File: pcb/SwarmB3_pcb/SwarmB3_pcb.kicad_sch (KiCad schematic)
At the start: 53 parts, among them J1 5v_3Pi, J10 ItsyBitsyRight, J11 ItsyBitsyLeft, J12 ItsyBitsyBottom, J2 GND_3Pi, J3 I2C_3V3_Exp, J4 Conn_02x15_M5Stack_Core2, J5 I2C_3Pi, J6 3PI_SWTCH, J8 ProxA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

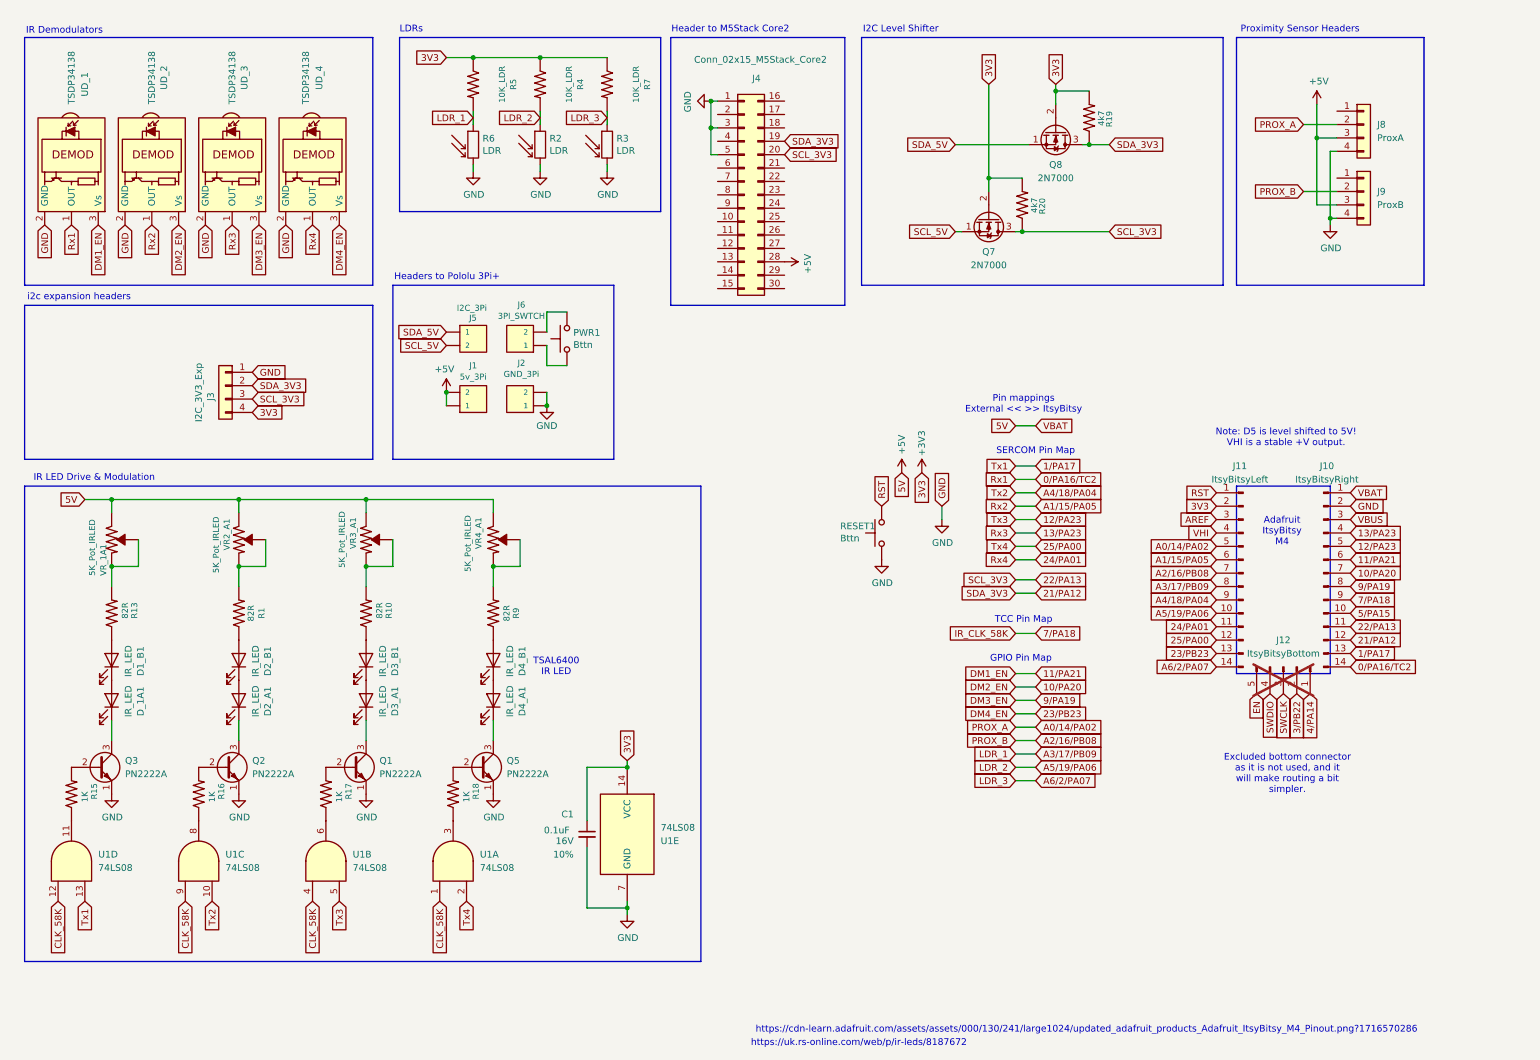
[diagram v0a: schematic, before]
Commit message: add initial test code for itsybitsy
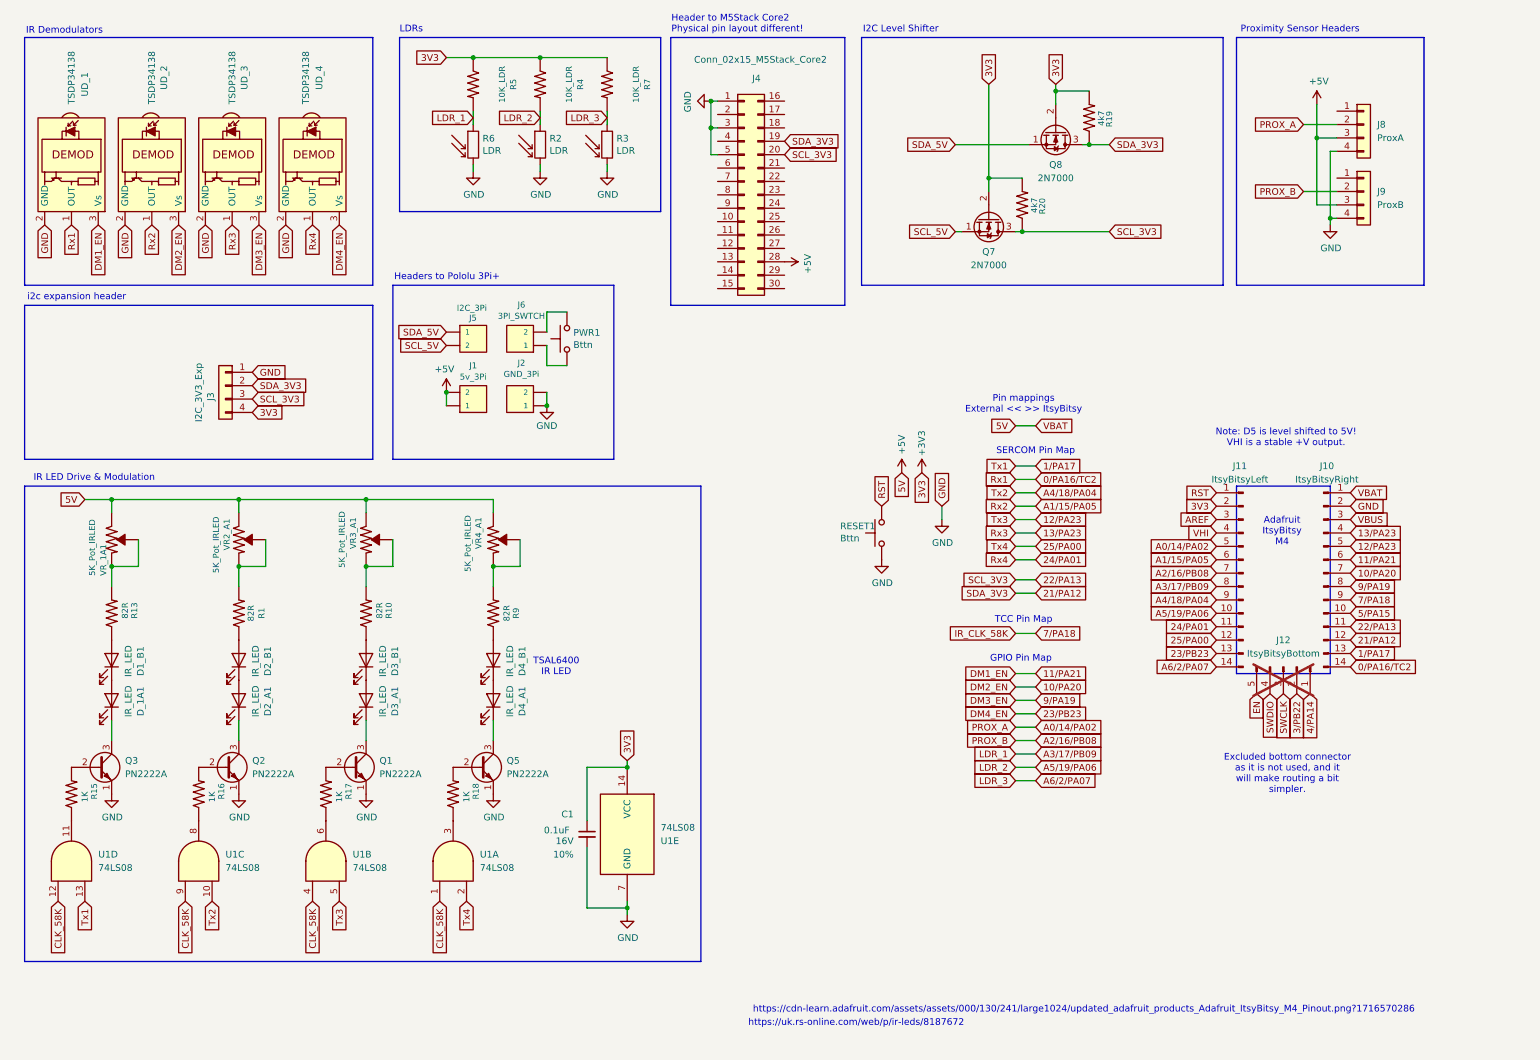
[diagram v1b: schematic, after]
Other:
- note added: "Header to M5Stack Core2 Physical pin layout different!"
- note added: "i2c expansion header"
- note removed: "Header to M5Stack Core2"
- note removed: "i2c expansion headers"
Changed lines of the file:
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@@
 		)
 	)
-	(text "Header to M5Stack Core2\n"
+	(text "Header to M5Stack Core2\nPhysical pin layout different!"
 		(exclude_from_sim no)
 		(at 136.652 17.018 0)
@@
 	(text "https://uk.rs-online.com/web/p/ir-leds/8187672"
 		(exclude_from_sim no)
-		(at 172.212 208.534 0)
+		(at 171.704 204.724 0)
 		(effects
 			(font
@@
 	(text "https://cdn-learn.adafruit.com/assets/assets/000/130/241/large1024/updated_adafruit_products_Adafruit_ItsyBitsy_M4_Pinout.png?1716570286"
 		(exclude_from_sim no)
-		(at 215.392 205.994 0)
+		(at 214.884 202.184 0)
 		(effects
 			(font
@@
 		)
 	)
-	(text "i2c expansion headers\n"
+	(text "i2c expansion header\n"
 		(exclude_from_sim no)
 		(at 14.478 67.818 0)

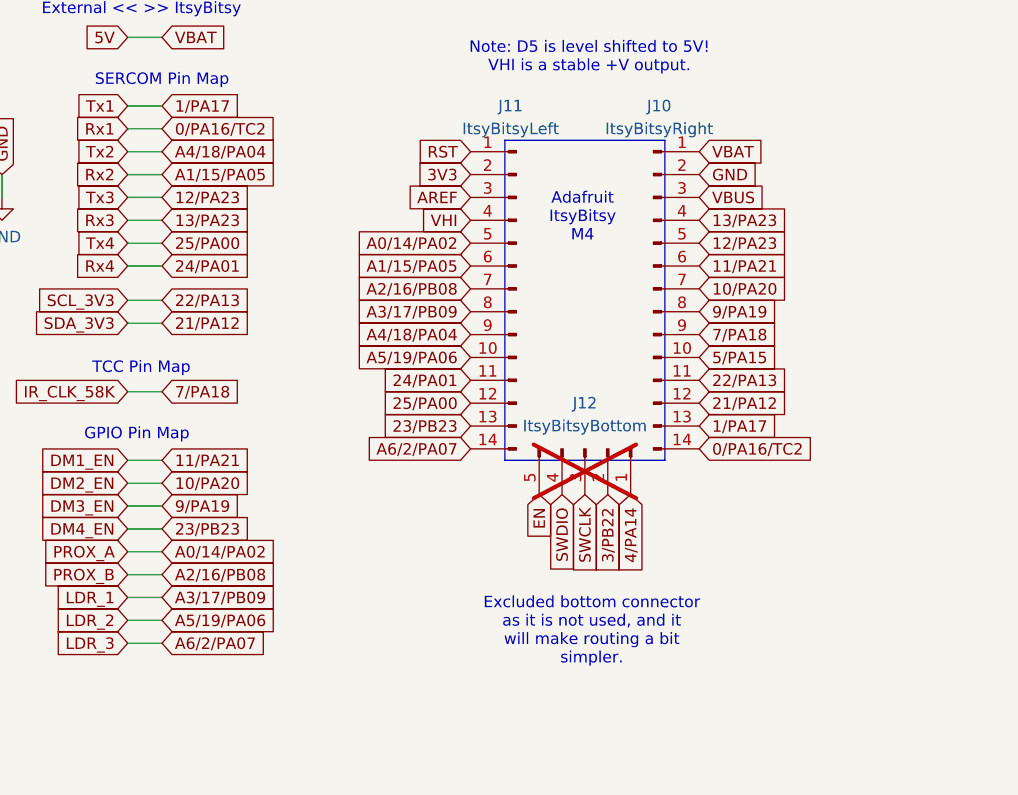
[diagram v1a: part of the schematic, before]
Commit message: tested i2c on default pins and a 58khz signal on pin 7, both working.
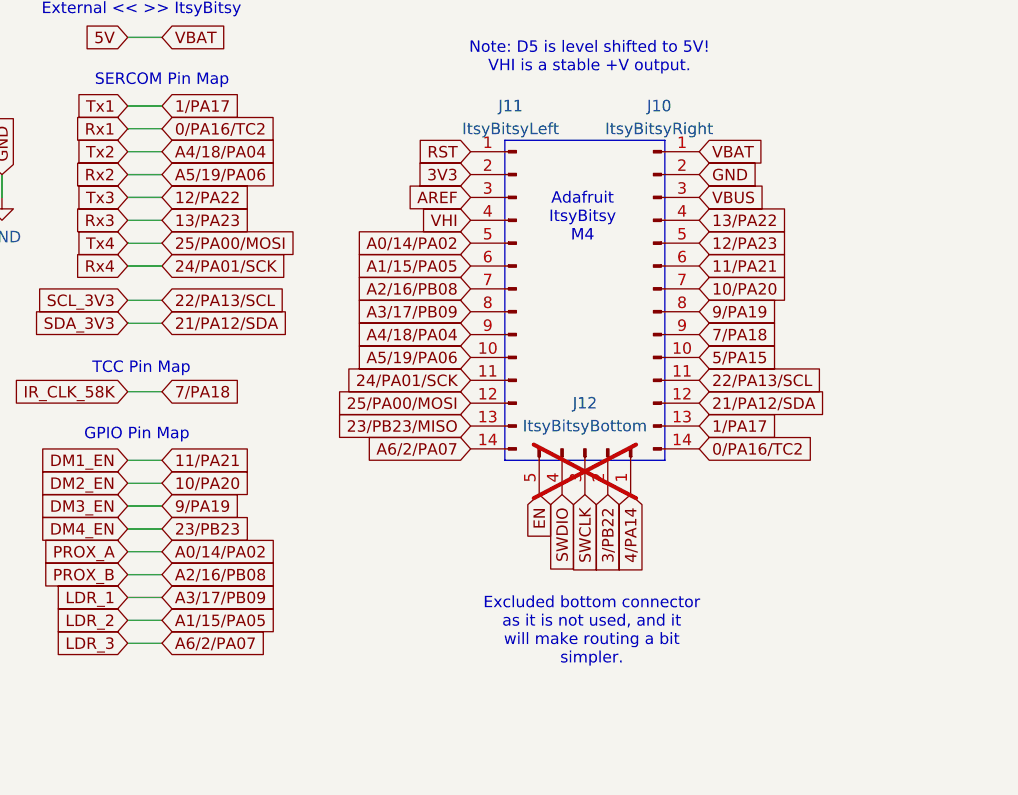
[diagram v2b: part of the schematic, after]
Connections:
- net 12/PA23: no longer U1.5
- net 13/PA23: no longer J10.4 (Pin_4)
- net 23/PB23: no longer J11.13 (Pin_13)
- net A1/15/PA05: now also R2.1, R4.2; no longer UD_2.1 (OUT)
- net A5/19/PA06: now also UD_2.1 (OUT); no longer R2.1, R4.2
- net 21/PA12 renamed 21/PA12/SDA
- net 22/PA13 renamed 22/PA13/SCL
- net 24/PA01 renamed 24/PA01/SCK
- net 25/PA00 renamed 25/PA00/MOSI
- new net 12/PA22: U1.5
- new net 13/PA22: J10.4 (Pin_4)
- new net 23/PB23/MISO: J11.13 (Pin_13)
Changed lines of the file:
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@@
 	(wire
 		(pts
-			(xy 201.93 106.68) (xy 205.74 106.68)
-		)
-		(stroke
-			(width 0)
-			(type default)
-		)
-	)
-	(wire
-		(pts
 			(xy 261.62 39.37) (xy 261.62 52.07)
 		)
@@
 	(wire
 		(pts
+			(xy 201.93 104.14) (xy 205.74 104.14)
+		)
+		(stroke
+			(width 0)
+			(type default)
+		)
+	)
+	(wire
+		(pts
 			(xy 259.08 49.53) (xy 259.08 36.83)
 		)
@@
 	(wire
 		(pts
-			(xy 201.93 156.21) (xy 205.74 156.21)
-		)
-		(stroke
-			(width 0)
-			(type default)
-		)
-	)
-	(wire
-		(pts
 			(xy 203.2 54.61) (xy 219.71 54.61)
 		)
@@
 	(wire
 		(pts
+			(xy 201.93 106.68) (xy 205.74 106.68)
+		)
+		(stroke
+			(width 0)
+			(type default)
+		)
+	)
+	(wire
+		(pts
 			(xy 35.56 113.03) (xy 35.56 118.11)
 		)
@@
 	(wire
 		(pts
-			(xy 128.27 184.15) (xy 128.27 182.88)
+			(xy 201.93 156.21) (xy 205.74 156.21)
 		)
 		(stroke
@@
 	(wire
 		(pts
-			(xy 201.93 104.14) (xy 205.74 104.14)
+			(xy 128.27 184.15) (xy 128.27 182.88)
 		)
 		(stroke
@@
 		)
 	)
-	(global_label "22{slash}PA13"
+	(global_label "22{slash}PA13{slash}SCL"
 		(shape input)
 		(at 205.74 120.65 0)
@@
 		)
 		(property "Intersheetrefs" "${INTERSHEET_REFS}"
-			(at 216.5981 120.65 0)
+			(at 221.4362 120.65 0)
 			(effects
 				(font
@@
 		)
 	)
-	(global_label "22{slash}PA13"
+	(global_label "22{slash}PA13{slash}SCL"
 		(shape input)
 		(at 265.43 129.54 0)
@@
 		)
 		(property "Intersheetrefs" "${INTERSHEET_REFS}"
-			(at 276.2881 129.54 0)
+			(at 281.1262 129.54 0)
 			(effects
 				(font
@@
 		)
 	)
-	(global_label "24{slash}PA01"
+	(global_label "24{slash}PA01{slash}SCK"
 		(shape input)
 		(at 205.74 116.84 0)
@@
 		)
 		(property "Intersheetrefs" "${INTERSHEET_REFS}"
-			(at 216.5981 116.84 0)
+			(at 221.6781 116.84 0)
 			(effects
 				(font
@@
 		)
 	)
-	(global_label "21{slash}PA12"
+	(global_label "21{slash}PA12{slash}SDA"
 		(shape input)
 		(at 265.43 132.08 0)
@@
 		)
 		(property "Intersheetrefs" "${INTERSHEET_REFS}"
-			(at 276.2881 132.08 0)
+			(at 281.1867 132.08 0)
 			(effects
 				(font
@@
 	(global_label "A1{slash}15{slash}PA05"
 		(shape input)
-		(at 205.74 106.68 0)
+		(at 205.74 156.21 0)
 		(fields_autoplaced yes)
 		(effects
@@
 		)
 		(property "Intersheetrefs" "${INTERSHEET_REFS}"
-			(at 220.2267 106.68 0)
+			(at 220.2267 156.21 0)
 			(effects
 				(font
@@
 		)
 	)
-	(global_label "13{slash}PA23"
+	(global_label "13{slash}PA22"
 		(shape input)
 		(at 265.43 111.76 0)
@@
 		)
 	)
-	(global_label "25{slash}PA00"
+	(global_label "25{slash}PA00{slash}MOSI"
 		(shape input)
 		(at 240.03 132.08 180)
@@
 		)
 		(property "Intersheetrefs" "${INTERSHEET_REFS}"
-			(at 229.1719 132.08 0)
+			(at 223.2452 132.08 0)
 			(effects
 				(font
@@
 		)
 	)
-	(global_label "23{slash}PB23"
+	(global_label "23{slash}PB23{slash}MISO"
 		(shape input)
 		(at 240.03 134.62 180)
@@
 		)
 		(property "Intersheetrefs" "${INTERSHEET_REFS}"
-			(at 228.9905 134.62 0)
+			(at 223.0638 134.62 0)
 			(effects
 				(font
@@
 		)
 	)
-	(global_label "25{slash}PA00"
+	(global_label "25{slash}PA00{slash}MOSI"
 		(shape input)
 		(at 205.74 114.3 0)
@@
 		)
 		(property "Intersheetrefs" "${INTERSHEET_REFS}"
-			(at 216.5981 114.3 0)
+			(at 222.5248 114.3 0)
 			(effects
 				(font
@@
 		)
 	)
-	(global_label "21{slash}PA12"
+	(global_label "21{slash}PA12{slash}SDA"
 		(shape input)
 		(at 205.74 123.19 0)
@@
 		)
 		(property "Intersheetrefs" "${INTERSHEET_REFS}"
-			(at 216.5981 123.19 0)
+			(at 221.4967 123.19 0)
 			(effects
 				(font
@@
 		)
 	)
-	(global_label "24{slash}PA01"
+	(global_label "24{slash}PA01{slash}SCK"
 		(shape input)
 		(at 240.03 129.54 180)
@@
 		)
 		(property "Intersheetrefs" "${INTERSHEET_REFS}"
-			(at 229.1719 129.54 0)
+			(at 224.0919 129.54 0)
 			(effects
 				(font
@@
 	(global_label "A5{slash}19{slash}PA06"
 		(shape input)
-		(at 205.74 156.21 0)
+		(at 205.74 106.68 0)
 		(fields_autoplaced yes)
 		(effects
@@
 		)
 		(property "Intersheetrefs" "${INTERSHEET_REFS}"
-			(at 220.2267 156.21 0)
+			(at 220.2267 106.68 0)
 			(effects
 				(font
@@
 		)
 	)
-	(global_label "12{slash}PA23"
+	(global_label "12{slash}PA22"
 		(shape input)
 		(at 205.74 109.22 0)

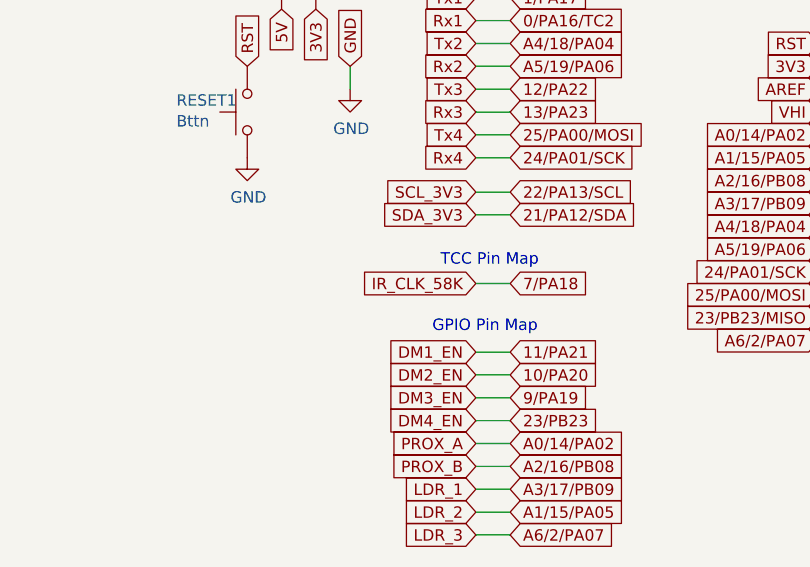
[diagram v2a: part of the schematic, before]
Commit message: Found errors with the PCB, fixed.  Pin 7 was labelled wrong, so it wasn't connected to the 74HC08.  3 of the pots were located in illogical places, not next to the associated LEDs.  The 74HC08 was also in it's own isolated ground network, but after fixing the other stuff, the new routing fixed the issue.
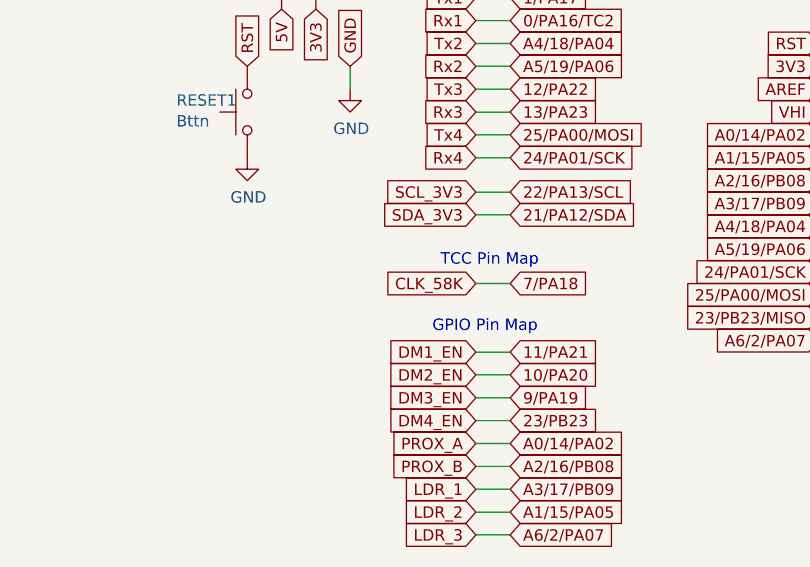
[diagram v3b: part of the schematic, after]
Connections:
- net CLK_58K is gone; now on net 7/PA18: U1.1, U1.12, U1.4, U1.9
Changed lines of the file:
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@@
 		)
 	)
-	(global_label "IR_CLK_58K"
+	(global_label "CLK_58K"
 		(shape input)
 		(at 201.93 130.81 180)
@@
 		)
 		(property "Intersheetrefs" "${INTERSHEET_REFS}"
-			(at 188.5319 130.81 0)
+			(at 191.3743 130.81 0)
 			(effects
 				(font

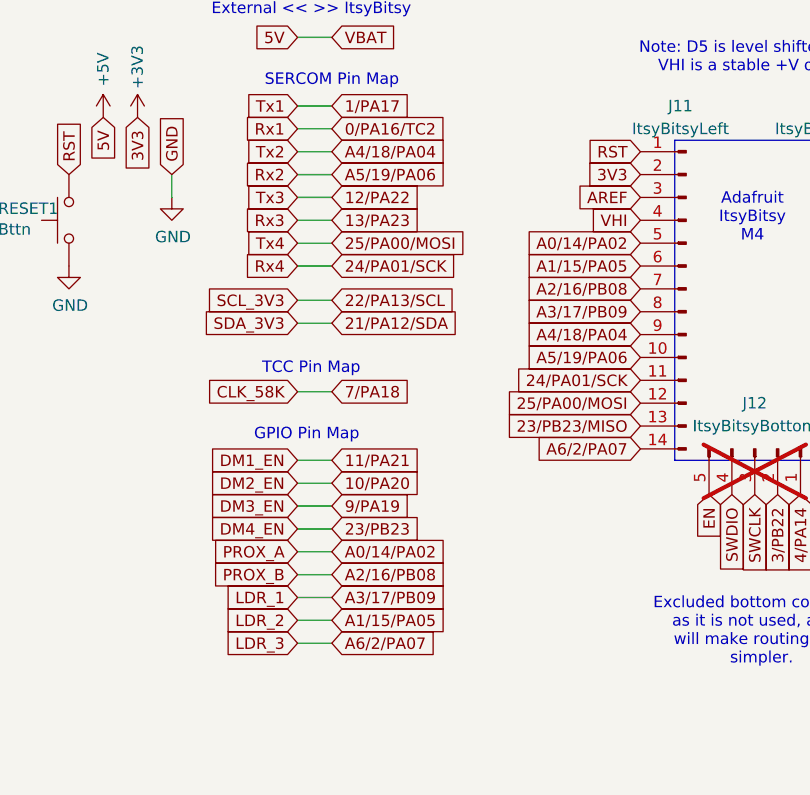
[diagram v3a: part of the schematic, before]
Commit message: Somehow, I had the pcb manufactured with A1 as rx for a UART, but my latest design files were for A5.  Since I've debugged and tested the PCB as working, I've modified the design files back to using A1.
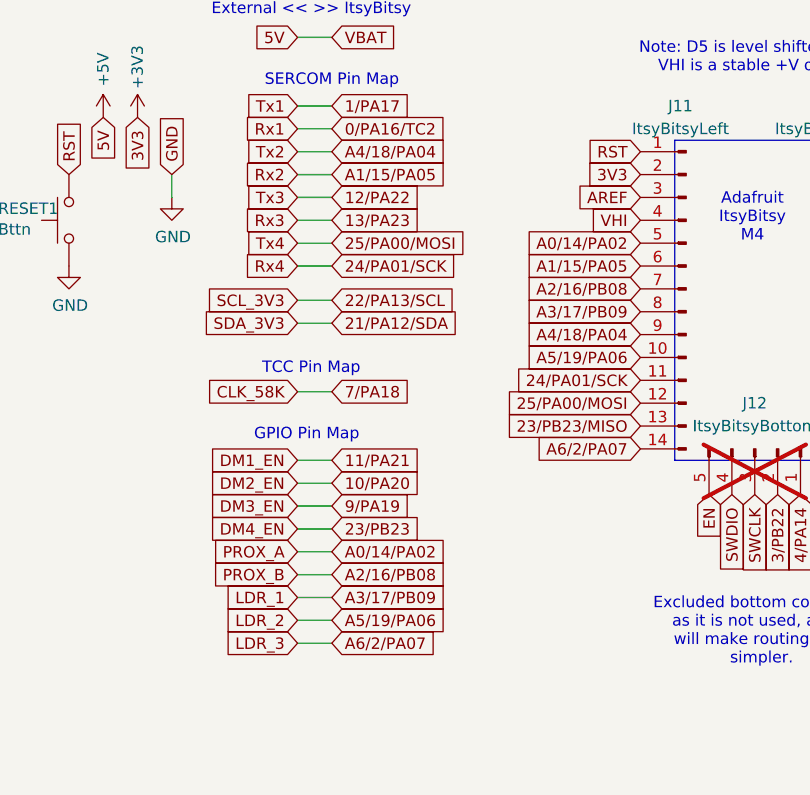
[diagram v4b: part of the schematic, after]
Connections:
- net A1/15/PA05: now also UD_2.1 (OUT); no longer R2.1, R4.2
- net A5/19/PA06: now also R2.1, R4.2; no longer UD_2.1 (OUT)
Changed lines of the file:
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@@
 	(wire
 		(pts
+			(xy 201.93 106.68) (xy 205.74 106.68)
+		)
+		(stroke
+			(width 0)
+			(type default)
+		)
+	)
+	(wire
+		(pts
 			(xy 201.93 146.05) (xy 205.74 146.05)
 		)
@@
 	(wire
 		(pts
-			(xy 201.93 106.68) (xy 205.74 106.68)
-		)
-		(stroke
-			(width 0)
-			(type default)
-		)
-	)
-	(wire
-		(pts
 			(xy 35.56 113.03) (xy 35.56 118.11)
 		)
@@
 	(wire
 		(pts
-			(xy 201.93 156.21) (xy 205.74 156.21)
-		)
-		(stroke
-			(width 0)
-			(type default)
-		)
-	)
-	(wire
-		(pts
 			(xy 128.27 184.15) (xy 128.27 182.88)
 		)
@@
 	(wire
 		(pts
+			(xy 201.93 156.21) (xy 205.74 156.21)
+		)
+		(stroke
+			(width 0)
+			(type default)
+		)
+	)
+	(wire
+		(pts
 			(xy 124.46 43.18) (xy 124.46 41.91)
 		)
@@
 	(global_label "A1{slash}15{slash}PA05"
 		(shape input)
-		(at 205.74 156.21 0)
+		(at 205.74 106.68 0)
 		(fields_autoplaced yes)
 		(effects
@@
 		)
 		(property "Intersheetrefs" "${INTERSHEET_REFS}"
-			(at 220.2267 156.21 0)
+			(at 220.2267 106.68 0)
 			(effects
 				(font
@@
 	(global_label "A5{slash}19{slash}PA06"
 		(shape input)
-		(at 205.74 106.68 0)
+		(at 205.74 156.21 0)
 		(fields_autoplaced yes)
 		(effects
@@
 		)
 		(property "Intersheetrefs" "${INTERSHEET_REFS}"
-			(at 220.2267 106.68 0)
+			(at 220.2267 156.21 0)
 			(effects
 				(font
